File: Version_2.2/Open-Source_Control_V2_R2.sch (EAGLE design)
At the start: 342 parts, among them IC10 MCP6002SMT, IC11 MCP6002SMT, IC12 MCP6002SMT, IC14 MCP6002SMT, IC2 ULN2003AD, IC4 74HC165D, IC5 74HC165D, J24 6p-2.54, K1 JS1-24V-F, K2 JS1-24V-F, K3 JS1-24V-F, K4 JS1-24V-F, K5 JS1-24V-F, Q1 MMBT2907, T4 DA2304-AL, U1 OSD3358-512M-ICB, U16 AT97SC3205T-G3M4400B, U2 TPD4S012_DRY_6_P1_M, U27 LAN8710, U28 TCAN1051HV, U29 MAX3483EESA+T, U4 APX811-31UGSOT, U40 ISO3086TDW, U5 TLVH431, U6 SN74LVC2G241_DCU_8, X1 10118194-0001LF, X10 MC4, X11 MC4, X12 MC4, X2 J0011D01BNL, X21 MC10, X24 MSTBA2, X3 MC4, X4 CTI-JTAG, X41 MSTBA3, X5 DM3CS-SF, X6 6p-2.54, X7 TH-2X10, X8 MC4, Y7 7A-25.000MAAE-T

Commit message: Add files via upload
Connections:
- removed net I2C1_SCL: R169.1, RTC1.SCL, TP20.TP, U1C.UART0_RTSN
- removed net I2C1_SDA: R170.1, RTC1.SDA, TP19.TP, U1C.UART0_CTSN
- new net I2C2_SCL: R169.1, RTC1.SCL, TP20.TP, U1C.UART1_RTSN
- new net I2C2_SDA: R170.1, RTC1.SDA, TP19.TP, U1C.UART1_CTSN
- net TPM_GPIO1: now also U1C.UART0_CTSN; no longer U1C.UART1_CTSN
- net TPM_GPIO2: now also U1C.UART0_RTSN; no longer U1C.UART1_RTSN
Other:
- moved on the sheet: TP10, TP19, TP20, TP9
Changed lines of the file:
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@@
 </text>
 <text x="10.16" y="104.14" size="2.54" layer="150">AT97SC3205T I2C Address:  0x29</text>
-<text x="797.56" y="127" size="2.54" layer="150">DS3231 I2C Address:  0x68</text>
+<text x="797.56" y="111.76" size="2.54" layer="150">DS3231 I2C Address:  0x68</text>
 <text x="760.73" y="1224.28" size="2.54" layer="94">2</text>
 <text x="369.57" y="1224.28" size="2.54" layer="94">2</text>
@@
 <attribute name="VALUE" x="850.9" y="152.4" size="1.778" layer="96"/>
 </instance>
-<instance part="TP9" gate="G$1" x="858.52" y="114.3" smashed="yes" rot="R180">
-<attribute name="NAME" x="845.82" y="114.3" size="1.778" layer="95"/>
+<instance part="TP9" gate="G$1" x="858.52" y="129.54" smashed="yes" rot="R180">
+<attribute name="NAME" x="845.82" y="129.54" size="1.778" layer="95"/>
 </instance>
-<instance part="TP10" gate="G$1" x="858.52" y="111.76" smashed="yes" rot="R180">
-<attribute name="NAME" x="845.82" y="111.76" size="1.778" layer="95"/>
+<instance part="TP10" gate="G$1" x="858.52" y="127" smashed="yes" rot="R180">
+<attribute name="NAME" x="845.82" y="127" size="1.778" layer="95"/>
 </instance>
 <instance part="R31" gate="G$1" x="1099.82" y="195.58" smashed="yes">
@@
 <attribute name="NAME" x="53.34" y="99.06" size="1.778" layer="95"/>
 </instance>
-<instance part="TP19" gate="G$1" x="858.52" y="129.54" smashed="yes" rot="R180">
-<attribute name="NAME" x="845.82" y="129.54" size="1.778" layer="95"/>
+<instance part="TP19" gate="G$1" x="858.52" y="114.3" smashed="yes" rot="R180">
+<attribute name="NAME" x="845.82" y="114.3" size="1.778" layer="95"/>
 </instance>
-<instance part="TP20" gate="G$1" x="858.52" y="127" smashed="yes" rot="R180">
-<attribute name="NAME" x="845.82" y="127" size="1.778" layer="95"/>
+<instance part="TP20" gate="G$1" x="858.52" y="111.76" smashed="yes" rot="R180">
+<attribute name="NAME" x="845.82" y="111.76" size="1.778" layer="95"/>
 </instance>
 <instance part="FRAME2" gate="G$1" x="784.86" y="1219.2" smashed="yes">
@@
 </segment>
 </net>
-<net name="I2C1_SDA" class="0">
-<segment>
-<pinref part="U1" gate="C" pin="UART0_CTSN"/>
-<wire x1="914.4" y1="129.54" x2="861.06" y2="129.54" width="0.1524" layer="91"/>
-<label x="861.06" y="129.54" size="1.778" layer="95"/>
-<pinref part="TP19" gate="G$1" pin="TP"/>
-</segment>
-<segment>
-<pinref part="RTC1" gate="G$1" pin="SDA"/>
-<wire x1="919.48" y1="482.6" x2="929.64" y2="482.6" width="0.1524" layer="91"/>
-<label x="932.18" y="482.6" size="1.778" layer="95"/>
-<pinref part="R170" gate="G$1" pin="1"/>
-<wire x1="929.64" y1="482.6" x2="942.34" y2="482.6" width="0.1524" layer="91"/>
-<wire x1="929.64" y1="487.68" x2="929.64" y2="482.6" width="0.1524" layer="91"/>
-<junction x="929.64" y="482.6"/>
-</segment>
-</net>
 <net name="USB0_P" class="0">
 <segment>
@@
 </segment>
 <segment>
-<pinref part="U1" gate="C" pin="UART1_CTSN"/>
-<wire x1="914.4" y1="114.3" x2="861.06" y2="114.3" width="0.1524" layer="91"/>
-<label x="861.06" y="114.3" size="1.778" layer="95"/>
+<pinref part="U1" gate="C" pin="UART0_CTSN"/>
 <pinref part="TP9" gate="G$1" pin="TP"/>
+<wire x1="914.4" y1="129.54" x2="861.06" y2="129.54" width="0.1524" layer="91"/>
+<label x="861.06" y="129.54" size="1.778" layer="95"/>
 </segment>
 </net>
@@
 </segment>
 <segment>
-<pinref part="U1" gate="C" pin="UART1_RTSN"/>
-<wire x1="914.4" y1="111.76" x2="861.06" y2="111.76" width="0.1524" layer="91"/>
-<label x="861.06" y="111.76" size="1.778" layer="95"/>
+<pinref part="U1" gate="C" pin="UART0_RTSN"/>
 <pinref part="TP10" gate="G$1" pin="TP"/>
+<wire x1="914.4" y1="127" x2="861.06" y2="127" width="0.1524" layer="91"/>
+<label x="861.06" y="127" size="1.778" layer="95"/>
 </segment>
 </net>
@@
 </segment>
 </net>
-<net name="I2C1_SCL" class="0">
-<segment>
-<pinref part="U1" gate="C" pin="UART0_RTSN"/>
-<wire x1="914.4" y1="127" x2="861.06" y2="127" width="0.1524" layer="91"/>
-<label x="861.06" y="127" size="1.778" layer="95"/>
-<pinref part="TP20" gate="G$1" pin="TP"/>
-</segment>
-<segment>
-<pinref part="RTC1" gate="G$1" pin="SCL"/>
-<wire x1="919.48" y1="485.14" x2="922.02" y2="485.14" width="0.1524" layer="91"/>
-<label x="932.18" y="485.14" size="1.778" layer="95"/>
-<pinref part="R169" gate="G$1" pin="1"/>
-<wire x1="922.02" y1="485.14" x2="942.34" y2="485.14" width="0.1524" layer="91"/>
-<wire x1="922.02" y1="487.68" x2="922.02" y2="485.14" width="0.1524" layer="91"/>
-<junction x="922.02" y="485.14"/>
-</segment>
-</net>
 <net name="N$10" class="0">
 <segment>
@@
 </segment>
 </net>
+<net name="I2C2_SCL" class="0">
+<segment>
+<pinref part="RTC1" gate="G$1" pin="SCL"/>
+<wire x1="919.48" y1="485.14" x2="922.02" y2="485.14" width="0.1524" layer="91"/>
+<label x="932.18" y="485.14" size="1.778" layer="95"/>
+<pinref part="R169" gate="G$1" pin="1"/>
+<wire x1="922.02" y1="485.14" x2="942.34" y2="485.14" width="0.1524" layer="91"/>
+<wire x1="922.02" y1="487.68" x2="922.02" y2="485.14" width="0.1524" layer="91"/>
+<junction x="922.02" y="485.14"/>
+</segment>
+<segment>
+<pinref part="U1" gate="C" pin="UART1_RTSN"/>
+<pinref part="TP20" gate="G$1" pin="TP"/>
+<wire x1="914.4" y1="111.76" x2="861.06" y2="111.76" width="0.1524" layer="91"/>
+<label x="861.06" y="111.76" size="1.778" layer="95"/>
+</segment>
+</net>
+<net name="I2C2_SDA" class="0">
+<segment>
+<pinref part="RTC1" gate="G$1" pin="SDA"/>
+<wire x1="919.48" y1="482.6" x2="929.64" y2="482.6" width="0.1524" layer="91"/>
+<label x="932.18" y="482.6" size="1.778" layer="95"/>
+<pinref part="R170" gate="G$1" pin="1"/>
+<wire x1="929.64" y1="482.6" x2="942.34" y2="482.6" width="0.1524" layer="91"/>
+<wire x1="929.64" y1="487.68" x2="929.64" y2="482.6" width="0.1524" layer="91"/>
+<junction x="929.64" y="482.6"/>
+</segment>
+<segment>
+<pinref part="U1" gate="C" pin="UART1_CTSN"/>
+<pinref part="TP19" gate="G$1" pin="TP"/>
+<wire x1="914.4" y1="114.3" x2="861.06" y2="114.3" width="0.1524" layer="91"/>
+<label x="861.06" y="114.3" size="1.778" layer="95"/>
+</segment>
+</net>

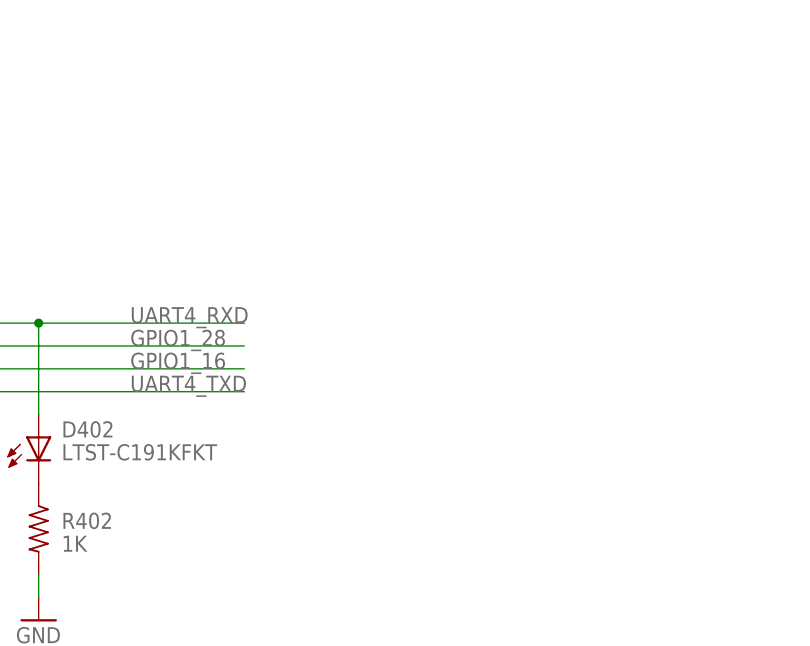
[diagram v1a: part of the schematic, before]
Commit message: Add files via upload
adding PRU UART option
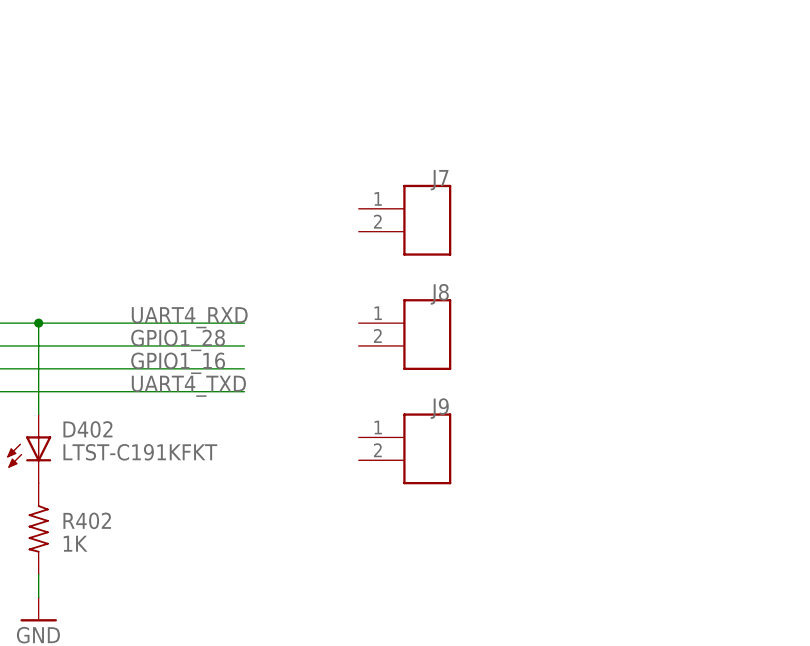
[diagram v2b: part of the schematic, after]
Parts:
- added J7, J8, J9: (no value), OSD3358-SM-RED Platform:826646-2
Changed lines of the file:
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@@
 <part name="TP20" library="OSD3358-SM-RED Platform" deviceset="TESTPAD/W_HOLE_1X1" device=""/>
 <part name="FRAME2" library="OSD3358-SM-RED Platform" deviceset="FRAMES_GEN" device=""/>
+<part name="J7" library="OSD3358-SM-RED Platform" deviceset="826646-2" device=""/>
+<part name="J8" library="OSD3358-SM-RED Platform" deviceset="826646-2" device=""/>
+<part name="J9" library="OSD3358-SM-RED Platform" deviceset="826646-2" device=""/>
 </parts>
 <sheets>
@@
 <attribute name="LAST_DATE_TIME" x="1098.55" y="1229.36" size="2.286" layer="94"/>
 </instance>
+<instance part="J7" gate="G$1" x="365.76" y="726.44" smashed="yes" rot="MR0">
+<attribute name="NAME" x="365.76" y="734.06" size="1.778" layer="95" ratio="10" rot="MR0"/>
+<attribute name="VALUE" x="365.76" y="723.9" size="1.778" layer="96" ratio="10" rot="MR0"/>
+</instance>
+<instance part="J8" gate="G$1" x="365.76" y="713.74" smashed="yes" rot="MR0">
+<attribute name="NAME" x="365.76" y="721.36" size="1.778" layer="95" ratio="10" rot="MR0"/>
+<attribute name="VALUE" x="365.76" y="711.2" size="1.778" layer="96" ratio="10" rot="MR0"/>
+</instance>
+<instance part="J9" gate="G$1" x="365.76" y="701.04" smashed="yes" rot="MR0">
+<attribute name="NAME" x="365.76" y="708.66" size="1.778" layer="95" ratio="10" rot="MR0"/>
+<attribute name="VALUE" x="365.76" y="698.5" size="1.778" layer="96" ratio="10" rot="MR0"/>
+</instance>
 </instances>

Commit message: Add files via upload
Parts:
- removed J7, J8, J9: (no value), OSD3358-SM-RED Platform:826646-2
- added J45, J450, J454: (no value), OSD3358-SM-RED Platform:826646-2
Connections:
- new net 485_RXD: D402.A, J45.1, U40.R
- new net 485_TXD: D401.A, J45.2, U40.D
- net CAN_H: now also X8.3.SK; no longer X8.2.SK
- net CAN_L: now also X8.2.SK; no longer X8.1.SK
- net GND: now also X8.1.SK; no longer X8.3.SK
- net GPIO1_16: no longer U40.DE
- net GPIO1_28: no longer U40.!RE
- net PR1_PRU0_PRU_R30_6: now also U40.!RE
- net PR1_PRU0_PRU_R30_7: now also U40.DE
- net PR1_UART0_RXD: now also J450.1
- net PR1_UART0_TXD: now also J450.2
- net UART4_RXD: now also J454.1; no longer D402.A, U40.R
- net UART4_TXD: now also J454.2; no longer D401.A, U40.D
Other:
- note added: "Use Jumpers to connect RS-485 to UART4 or PRU1 UART0"
- moved on the sheet: X8.1, X8.2, X8.3
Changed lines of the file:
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@@
 <part name="TP20" library="OSD3358-SM-RED Platform" deviceset="TESTPAD/W_HOLE_1X1" device=""/>
 <part name="FRAME2" library="OSD3358-SM-RED Platform" deviceset="FRAMES_GEN" device=""/>
-<part name="J7" library="OSD3358-SM-RED Platform" deviceset="826646-2" device=""/>
-<part name="J8" library="OSD3358-SM-RED Platform" deviceset="826646-2" device=""/>
-<part name="J9" library="OSD3358-SM-RED Platform" deviceset="826646-2" device=""/>
+<part name="J454" library="OSD3358-SM-RED Platform" deviceset="826646-2" device=""/>
+<part name="J45" library="OSD3358-SM-RED Platform" deviceset="826646-2" device=""/>
+<part name="J450" library="OSD3358-SM-RED Platform" deviceset="826646-2" device=""/>
 </parts>
 <sheets>
@@
 <text x="815.34" y="1427.48" size="2.54" layer="150">Rev 1:
     1)  Revised Prototype.</text>
+<text x="342.9" y="685.8" size="2.54" layer="150">Use Jumpers to connect
+RS-485 to UART4 or
+PRU1 UART0</text>
 </plain>
 <instances>
@@
 <attribute name="VALUE" x="485.14" y="322.58" size="1.778" layer="96" align="top-right"/>
 </instance>
-<instance part="X8" gate=".1" x="998.22" y="683.26" smashed="yes" rot="MR0">
+<instance part="X8" gate=".1" x="335.28" y="1016" smashed="yes" rot="MR0">
+<attribute name="NAME" x="342.9" y="1017.905" size="1.524" layer="95" rot="MR0"/>
+</instance>
+<instance part="X8" gate=".2" x="998.22" y="683.26" smashed="yes" rot="MR0">
 <attribute name="NAME" x="1005.84" y="685.165" size="1.524" layer="95" rot="MR0"/>
 </instance>
-<instance part="X8" gate=".2" x="998.22" y="693.42" smashed="yes" rot="MR0">
+<instance part="X8" gate=".3" x="998.22" y="693.42" smashed="yes" rot="MR0">
 <attribute name="NAME" x="1005.84" y="695.325" size="1.524" layer="95" rot="MR0"/>
 </instance>
-<instance part="X8" gate=".3" x="335.28" y="1016" smashed="yes" rot="MR0">
-<attribute name="NAME" x="342.9" y="1017.905" size="1.524" layer="95" rot="MR0"/>
-</instance>
 <instance part="X8" gate=".4" x="335.28" y="1021.08" smashed="yes" rot="MR0">
 <attribute name="NAME" x="342.9" y="1022.985" size="1.524" layer="95" rot="MR0"/>
@@
 <attribute name="LAST_DATE_TIME" x="1098.55" y="1229.36" size="2.286" layer="94"/>
 </instance>
-<instance part="J7" gate="G$1" x="365.76" y="726.44" smashed="yes" rot="MR0">
-<attribute name="NAME" x="365.76" y="734.06" size="1.778" layer="95" ratio="10" rot="MR0"/>
-<attribute name="VALUE" x="365.76" y="723.9" size="1.778" layer="96" ratio="10" rot="MR0"/>
-</instance>
-<instance part="J8" gate="G$1" x="365.76" y="713.74" smashed="yes" rot="MR0">
-<attribute name="NAME" x="365.76" y="721.36" size="1.778" layer="95" ratio="10" rot="MR0"/>
-<attribute name="VALUE" x="365.76" y="711.2" size="1.778" layer="96" ratio="10" rot="MR0"/>
-</instance>
-<instance part="J9" gate="G$1" x="365.76" y="701.04" smashed="yes" rot="MR0">
-<attribute name="NAME" x="365.76" y="708.66" size="1.778" layer="95" ratio="10" rot="MR0"/>
-<attribute name="VALUE" x="365.76" y="698.5" size="1.778" layer="96" ratio="10" rot="MR0"/>
+<instance part="J454" gate="G$1" x="347.98" y="721.36" smashed="yes">
+<attribute name="NAME" x="347.98" y="728.98" size="1.778" layer="95" ratio="10"/>
+<attribute name="VALUE" x="347.98" y="718.82" size="1.778" layer="96" ratio="10"/>
+</instance>
+<instance part="J45" gate="G$1" x="353.06" y="711.2" smashed="yes" rot="MR0">
+<attribute name="NAME" x="353.06" y="718.82" size="1.778" layer="95" ratio="10" rot="MR0"/>
+<attribute name="VALUE" x="353.06" y="708.66" size="1.778" layer="96" ratio="10" rot="MR0"/>
+</instance>
+<instance part="J450" gate="G$1" x="347.98" y="701.04" smashed="yes">
+<attribute name="NAME" x="347.98" y="708.66" size="1.778" layer="95" ratio="10"/>
+<attribute name="VALUE" x="347.98" y="698.5" size="1.778" layer="96" ratio="10"/>
 </instance>
 </instances>
@@
 </segment>
 <segment>
-<pinref part="X8" gate=".3" pin="SK"/>
-<wire x1="335.28" y1="1016" x2="325.12" y2="1016" width="0.1524" layer="91"/>
 <pinref part="GND23" gate="1" pin="GND"/>
 <wire x1="325.12" y1="1016" x2="325.12" y2="1005.84" width="0.1524" layer="91"/>
+<pinref part="X8" gate=".1" pin="SK"/>
+<wire x1="325.12" y1="1016" x2="335.28" y2="1016" width="0.1524" layer="91"/>
 </segment>
 <segment>
@@
 </segment>
 <segment>
-<pinref part="U40" gate="A" pin="R"/>
-<wire x1="259.08" y1="718.82" x2="320.04" y2="718.82" width="0.1524" layer="91"/>
-<label x="330.2" y="718.82" size="1.778" layer="95"/>
-<pinref part="D402" gate="G$1" pin="A"/>
-<wire x1="320.04" y1="718.82" x2="342.9" y2="718.82" width="0.1524" layer="91"/>
-<wire x1="320.04" y1="708.66" x2="320.04" y2="718.82" width="0.1524" layer="91"/>
-<junction x="320.04" y="718.82"/>
+<pinref part="J454" gate="G$1" pin="1"/>
+<wire x1="358.14" y1="726.44" x2="381" y2="726.44" width="0.1524" layer="91"/>
+<label x="365.76" y="726.44" size="1.778" layer="95"/>
 </segment>
 </net>
@@
 </segment>
 <segment>
-<pinref part="U40" gate="A" pin="D"/>
-<wire x1="259.08" y1="711.2" x2="294.64" y2="711.2" width="0.1524" layer="91"/>
-<label x="330.2" y="711.2" size="1.778" layer="95"/>
-<pinref part="D401" gate="G$1" pin="A"/>
-<wire x1="294.64" y1="711.2" x2="342.9" y2="711.2" width="0.1524" layer="91"/>
-<wire x1="294.64" y1="708.66" x2="294.64" y2="711.2" width="0.1524" layer="91"/>
-<junction x="294.64" y="711.2"/>
+<pinref part="J454" gate="G$1" pin="2"/>
+<wire x1="358.14" y1="723.9" x2="381" y2="723.9" width="0.1524" layer="91"/>
+<label x="365.76" y="723.9" size="1.778" layer="95"/>
 </segment>
 </net>
@@
 <label x="1018.54" y="96.52" size="1.778" layer="95"/>
 </segment>
-<segment>
-<pinref part="U40" gate="A" pin="!RE"/>
-<wire x1="259.08" y1="716.28" x2="342.9" y2="716.28" width="0.1524" layer="91"/>
-<label x="330.2" y="716.28" size="1.778" layer="95"/>
-</segment>
 </net>
 <net name="GPIO1_12" class="0">
@@
 <net name="GPIO1_16" class="0">
 <segment>
-<pinref part="U40" gate="A" pin="DE"/>
-<label x="330.2" y="713.74" size="1.778" layer="95"/>
-<wire x1="259.08" y1="713.74" x2="342.9" y2="713.74" width="0.1524" layer="91"/>
-</segment>
-<segment>
 <pinref part="U1" gate="C" pin="GPMC_CSN3"/>
 <wire x1="975.36" y1="81.28" x2="1031.24" y2="81.28" width="0.1524" layer="91"/>
@@
 <pinref part="D805" gate="G$1" pin="2"/>
 <wire x1="980.44" y1="680.72" x2="980.44" y2="693.42" width="0.1524" layer="91"/>
-<pinref part="X8" gate=".2" pin="SK"/>
-<wire x1="998.22" y1="693.42" x2="980.44" y2="693.42" width="0.1524" layer="91"/>
+<pinref part="X8" gate=".3" pin="SK"/>
+<wire x1="980.44" y1="693.42" x2="998.22" y2="693.42" width="0.1524" layer="91"/>
 <junction x="980.44" y="693.42"/>
 </segment>
@@
 <pinref part="D805" gate="G$1" pin="1"/>
 <wire x1="990.6" y1="680.72" x2="990.6" y2="683.26" width="0.1524" layer="91"/>
-<pinref part="X8" gate=".1" pin="SK"/>
-<wire x1="998.22" y1="683.26" x2="990.6" y2="683.26" width="0.1524" layer="91"/>
+<pinref part="X8" gate=".2" pin="SK"/>
+<wire x1="990.6" y1="683.26" x2="998.22" y2="683.26" width="0.1524" layer="91"/>
 <junction x="990.6" y="683.26"/>
 </segment>
@@
 <label x="861.06" y="96.52" size="1.778" layer="95"/>
 </segment>
+<segment>
+<pinref part="J450" gate="G$1" pin="2"/>
+<wire x1="358.14" y1="703.58" x2="381" y2="703.58" width="0.1524" layer="91"/>
+<label x="360.68" y="703.58" size="1.778" layer="95"/>
+</segment>
 </net>
 <net name="PR1_PRU0_PRU_R30_7" class="0">
@@
 <label x="861.06" y="48.26" size="1.778" layer="95"/>
 </segment>
+<segment>
+<pinref part="U40" gate="A" pin="DE"/>
+<wire x1="259.08" y1="713.74" x2="314.96" y2="713.74" width="0.1524" layer="91"/>
+<label x="287.02" y="713.74" size="1.778" layer="95"/>
+</segment>
 </net>
 <net name="PR1_PRU0_PRU_R30_6" class="0">
@@
 <label x="861.06" y="50.8" size="1.778" layer="95"/>
 </segment>
+<segment>
+<pinref part="U40" gate="A" pin="!RE"/>
+<wire x1="259.08" y1="716.28" x2="314.96" y2="716.28" width="0.1524" layer="91"/>
+<label x="287.02" y="716.28" size="1.778" layer="95"/>
+</segment>
 </net>
 <net name="PR1_UART0_RXD" class="0">
@@
 <label x="861.06" y="99.06" size="1.778" layer="95"/>
 </segment>
+<segment>
+<pinref part="J450" gate="G$1" pin="1"/>
+<wire x1="358.14" y1="706.12" x2="381" y2="706.12" width="0.1524" layer="91"/>
+<label x="360.68" y="706.12" size="1.778" layer="95"/>
+</segment>
 </net>
 <net name="GPIO0_7" class="0">
@@
 </segment>
 </net>
+<net name="485_RXD" class="0">
+<segment>
+<pinref part="U40" gate="A" pin="R"/>
+<wire x1="259.08" y1="718.82" x2="320.04" y2="718.82" width="0.1524" layer="91"/>
+<label x="325.12" y="718.82" size="1.778" layer="95"/>
+<pinref part="D402" gate="G$1" pin="A"/>
+<wire x1="320.04" y1="718.82" x2="340.36" y2="718.82" width="0.1524" layer="91"/>
+<wire x1="320.04" y1="708.66" x2="320.04" y2="718.82" width="0.1524" layer="91"/>
+<junction x="320.04" y="718.82"/>
+<pinref part="J45" gate="G$1" pin="1"/>
+<wire x1="342.9" y1="716.28" x2="340.36" y2="716.28" width="0.1524" layer="91"/>
+<wire x1="340.36" y1="716.28" x2="340.36" y2="718.82" width="0.1524" layer="91"/>
+</segment>
+</net>
+<net name="485_TXD" class="0">
+<segment>
+<pinref part="U40" gate="A" pin="D"/>
+<wire x1="259.08" y1="711.2" x2="294.64" y2="711.2" width="0.1524" layer="91"/>
+<label x="325.12" y="711.2" size="1.778" layer="95"/>
+<pinref part="D401" gate="G$1" pin="A"/>
+<wire x1="294.64" y1="711.2" x2="340.36" y2="711.2" width="0.1524" layer="91"/>
+<wire x1="294.64" y1="708.66" x2="294.64" y2="711.2" width="0.1524" layer="91"/>
+<junction x="294.64" y="711.2"/>
+<pinref part="J45" gate="G$1" pin="2"/>
+<wire x1="342.9" y1="713.74" x2="340.36" y2="713.74" width="0.1524" layer="91"/>
+<wire x1="340.36" y1="713.74" x2="340.36" y2="711.2" width="0.1524" layer="91"/>
+</segment>
+</net>
